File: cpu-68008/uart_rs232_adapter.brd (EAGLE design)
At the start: 65.7 x 44.9 mm, 19 parts, among them IC1 MAX232

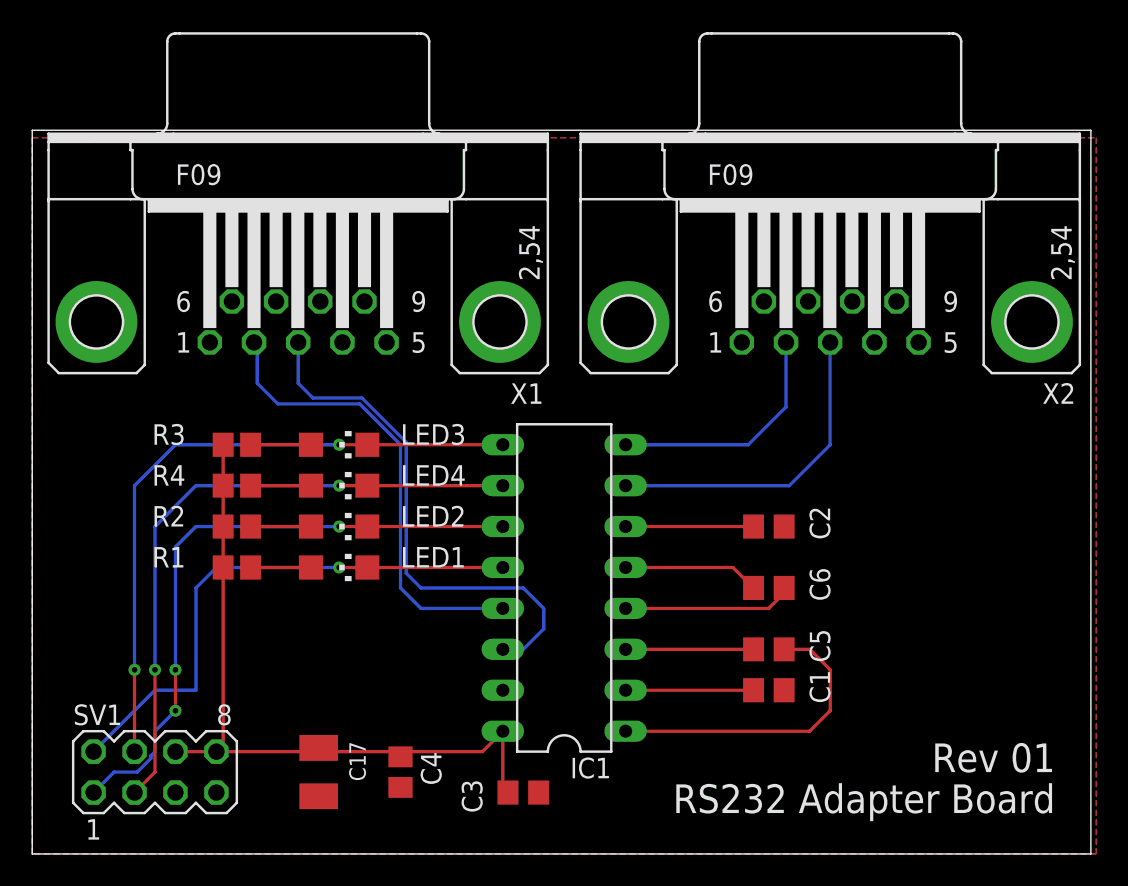
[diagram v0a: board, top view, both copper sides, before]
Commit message: rev 01 boards for cpu-68008 sent to fab
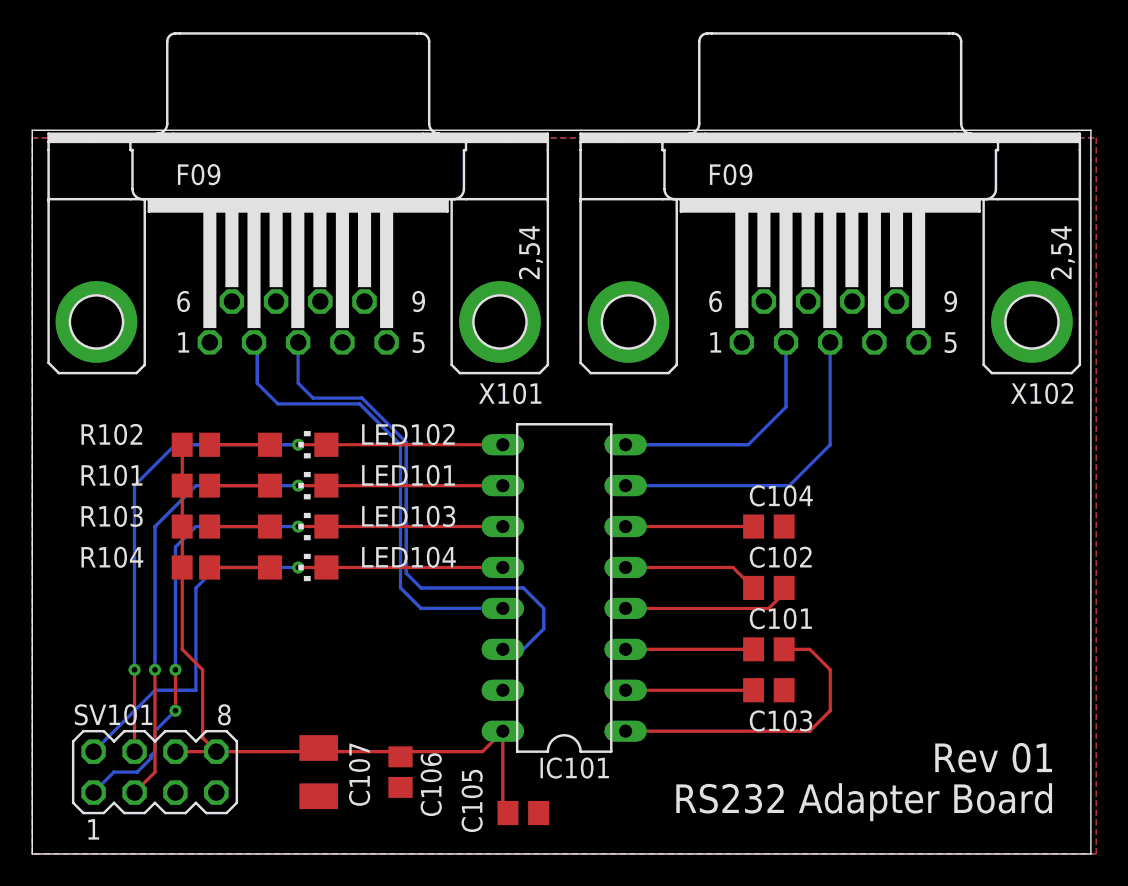
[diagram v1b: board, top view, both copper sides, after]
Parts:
- removed C3: 100nF, rcl:C0805
- removed LED1, LED2, LED3, LED4: (no value), led:CHIPLED_1206
- removed R1, R2, R3, R4: 3k, rcl:R2012
- added C105: 100nF, rcl:C0805
- added LED101, LED102, LED103, LED104: (no value), led:CHIPLED_1206
- added R101, R102, R103, R104: 3k, rcl:R2012
- renumbered C1 to C103, C17 to C107, C2 to C104, C4 to C106, C5 to C101, C6 to C102, IC1 to IC101, SV1 to SV101, X1 to X101, X2 to X102
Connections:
- net +5V: now also C105.1, R101.1, R102.1, R103.1, R104.1; no longer C3.1, R1.1, R2.1, R3.1, R4.1
- net GND: now also C105.2; no longer C3.2
- net N$1: now also LED104.A, R104.2; no longer LED1.A, R1.2
- net N$2: now also LED103.A, R103.2; no longer LED2.A, R2.2
- net N$3: now also LED102.A, R102.2; no longer LED3.A, R3.2
- net N$5: now also LED101.A, R101.2; no longer LED4.A, R4.2
- net UART0_RX: now also LED104.C; no longer LED1.C
- net UART0_TX: now also LED103.C; no longer LED2.C
- net UART1_RX: now also LED102.C; no longer LED3.C
- net UART1_TX: now also LED101.C; no longer LED4.C
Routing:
- net +5V: track 44.6 -> 46.5 mm
